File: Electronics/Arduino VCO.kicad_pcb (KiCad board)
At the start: 2 copper layers, 61 parts, among them J5 Conn_02x08_Odd_Even, U1 TL072

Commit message: deleting unused files
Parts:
- moved R1 39.1 mm to (115.6, 57.1)
- moved R10 39.1 mm to (120.3, 65.9)
- moved R11 39.1 mm to (120.3, 68.9)
- moved R12 39.1 mm to (120.3, 71.8)
- moved R13 39.1 mm to (125.1, 57.1)
- moved R14 39.1 mm to (125.1, 60.0)
- moved R15 39.1 mm to (125.1, 63.0)
- moved R16 39.1 mm to (125.1, 65.9)
- moved R17 39.1 mm to (125.1, 68.9)
- moved R2 39.1 mm to (115.6, 60.0)
- moved R3 39.1 mm to (115.6, 63.0)
- moved R4 39.1 mm to (115.6, 65.9)
- moved R5 39.1 mm to (115.6, 68.9)
- moved R6 39.1 mm to (115.6, 71.8)
- moved R7 39.1 mm to (120.3, 57.1)
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
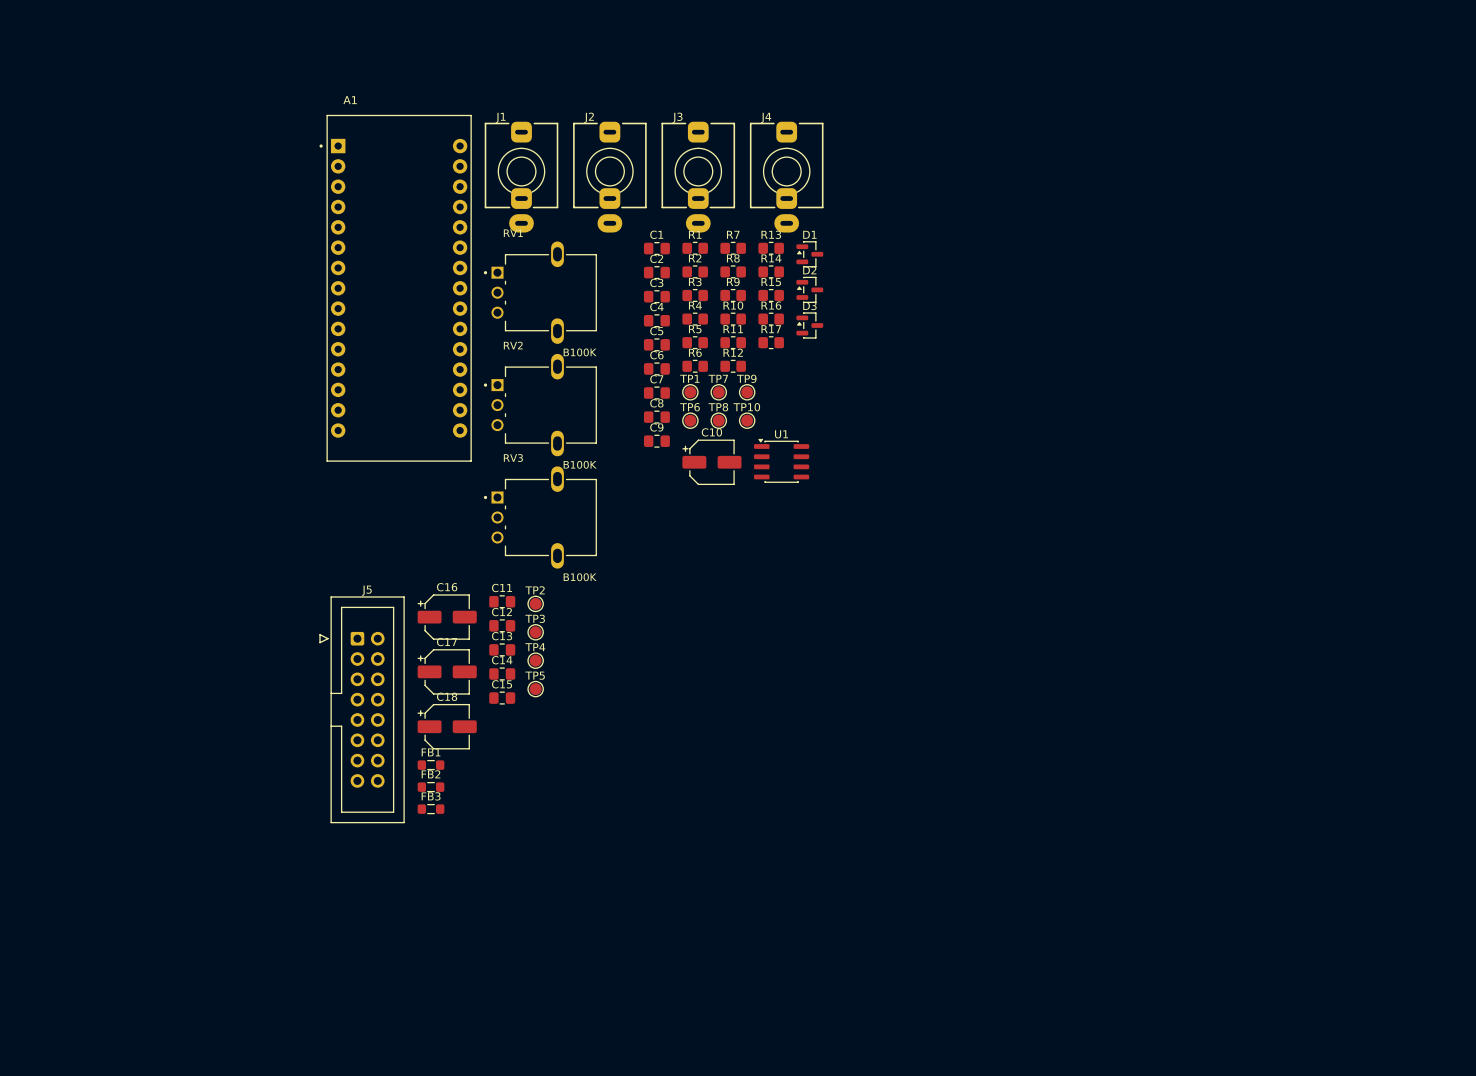
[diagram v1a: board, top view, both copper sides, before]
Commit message: creating a 6HP PCB panel
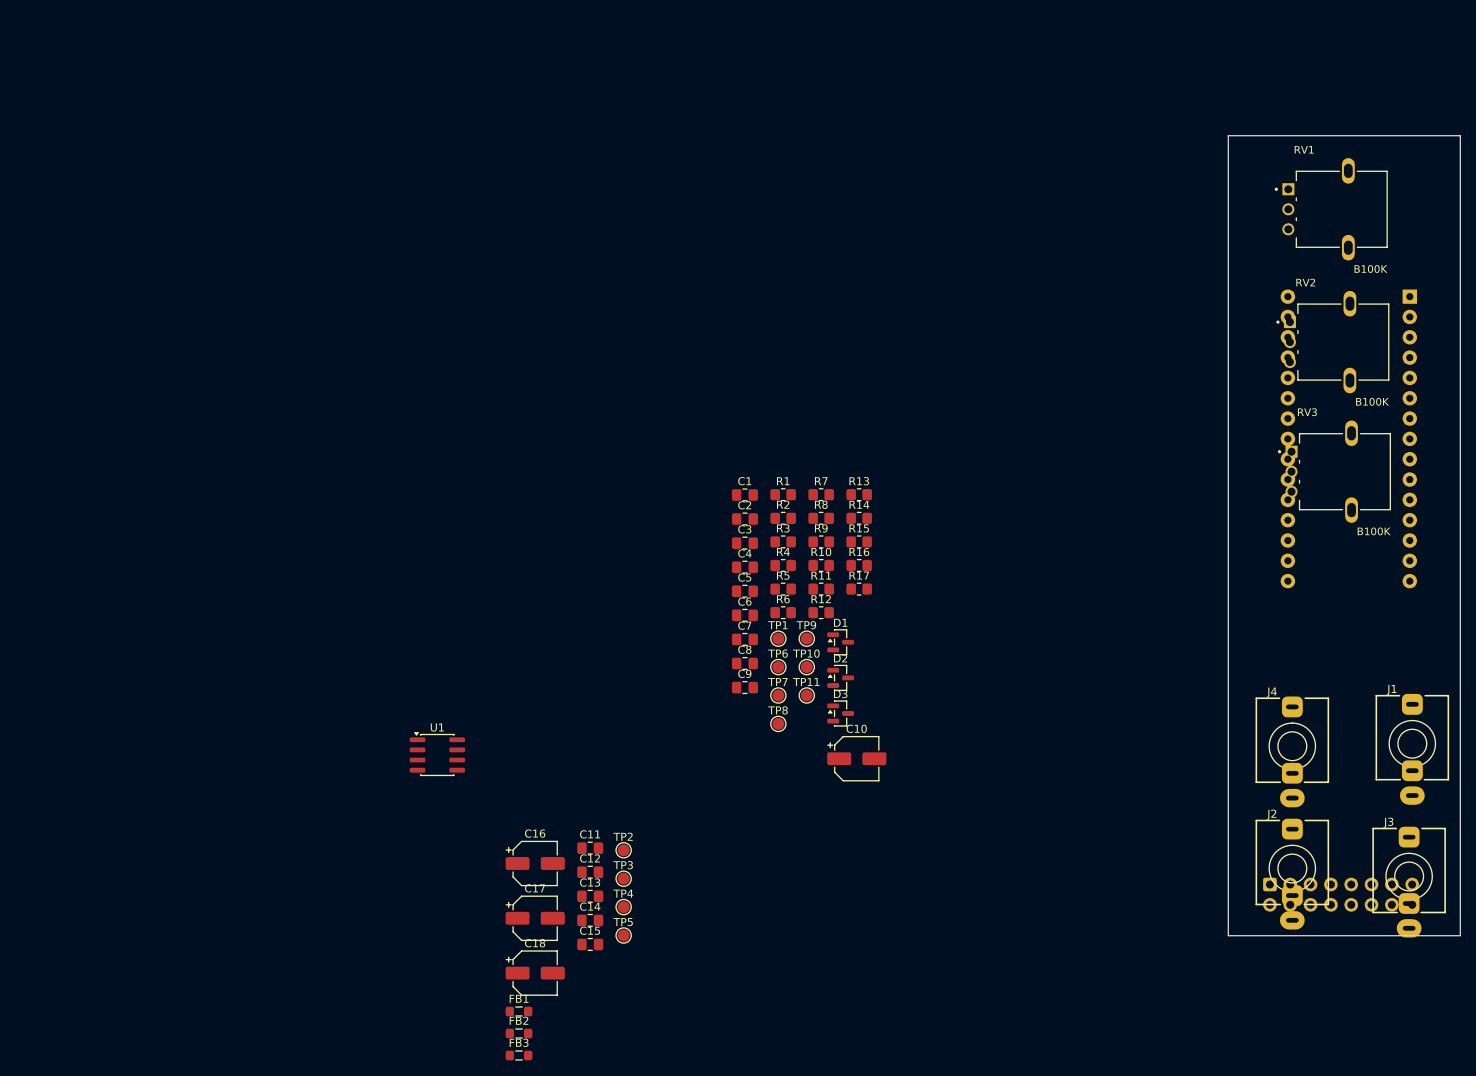
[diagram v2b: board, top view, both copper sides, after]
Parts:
- added TP11: C, TestPoint:TestPoint_Pad_D1.5mm, F.Cu at (129.5, 113.0)
- A1, J5: moved to B.Cu
- moved J1 132.3 mm to (205.2, 119.0)
- moved J3 125.1 mm to (204.8, 135.6)
- moved J2 121.9 mm to (190.2, 134.6)
- moved A1 120.2 mm to (197.3, 80.9), turned to 180 degrees
- moved J5 118.1 mm to (187.4, 136.6), turned to -90 degrees
- moved RV3 99.4 mm to (197.6, 85.0)
- moved RV1 99.4 mm to (197.2, 52.2)
- moved RV2 99.4 mm to (197.4, 68.8)
- moved J4 95.7 mm to (190.2, 119.3)
- moved U1 56.5 mm to (83.3, 120.4)
- moved D2 48.7 mm to (133.7, 110.8)
- moved D1 48.7 mm to (133.7, 106.3)
- moved D3 48.7 mm to (133.7, 115.2)
- moved C10 41.2 mm to (135.8, 120.9)
- moved TP8 38.6 mm to (126.0, 116.5)
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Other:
- board outline added: 29 x 100 mm
